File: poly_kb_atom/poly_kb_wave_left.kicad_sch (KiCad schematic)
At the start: 49 parts, among them U1 Pico, U2 TD6811, U3 MT9700

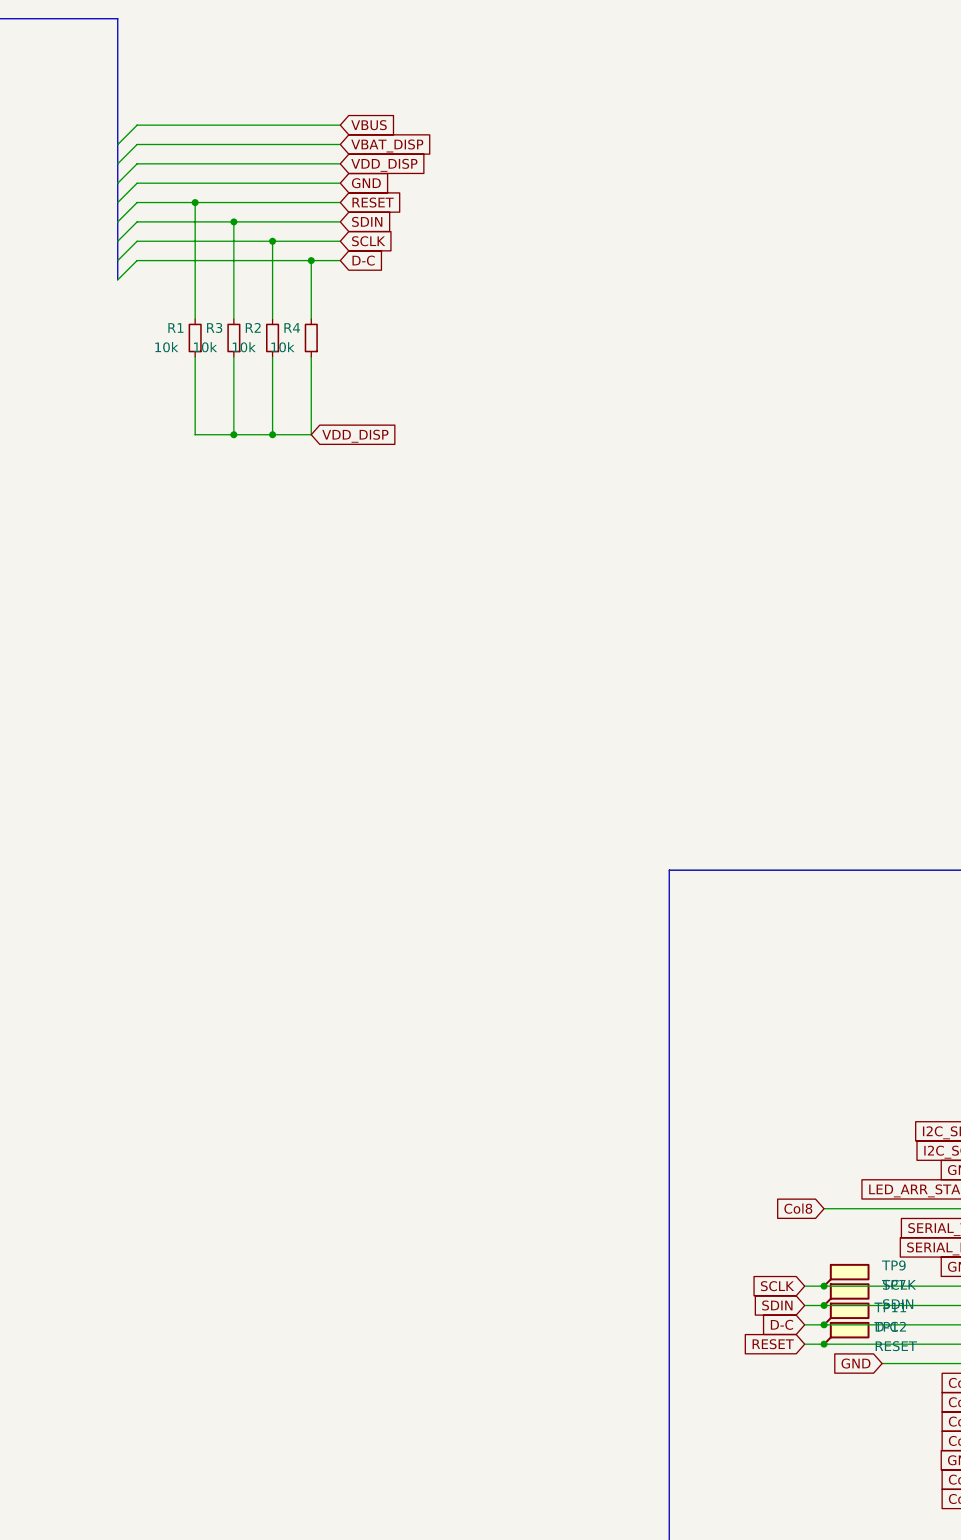
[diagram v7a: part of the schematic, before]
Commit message: Optional termination resistors
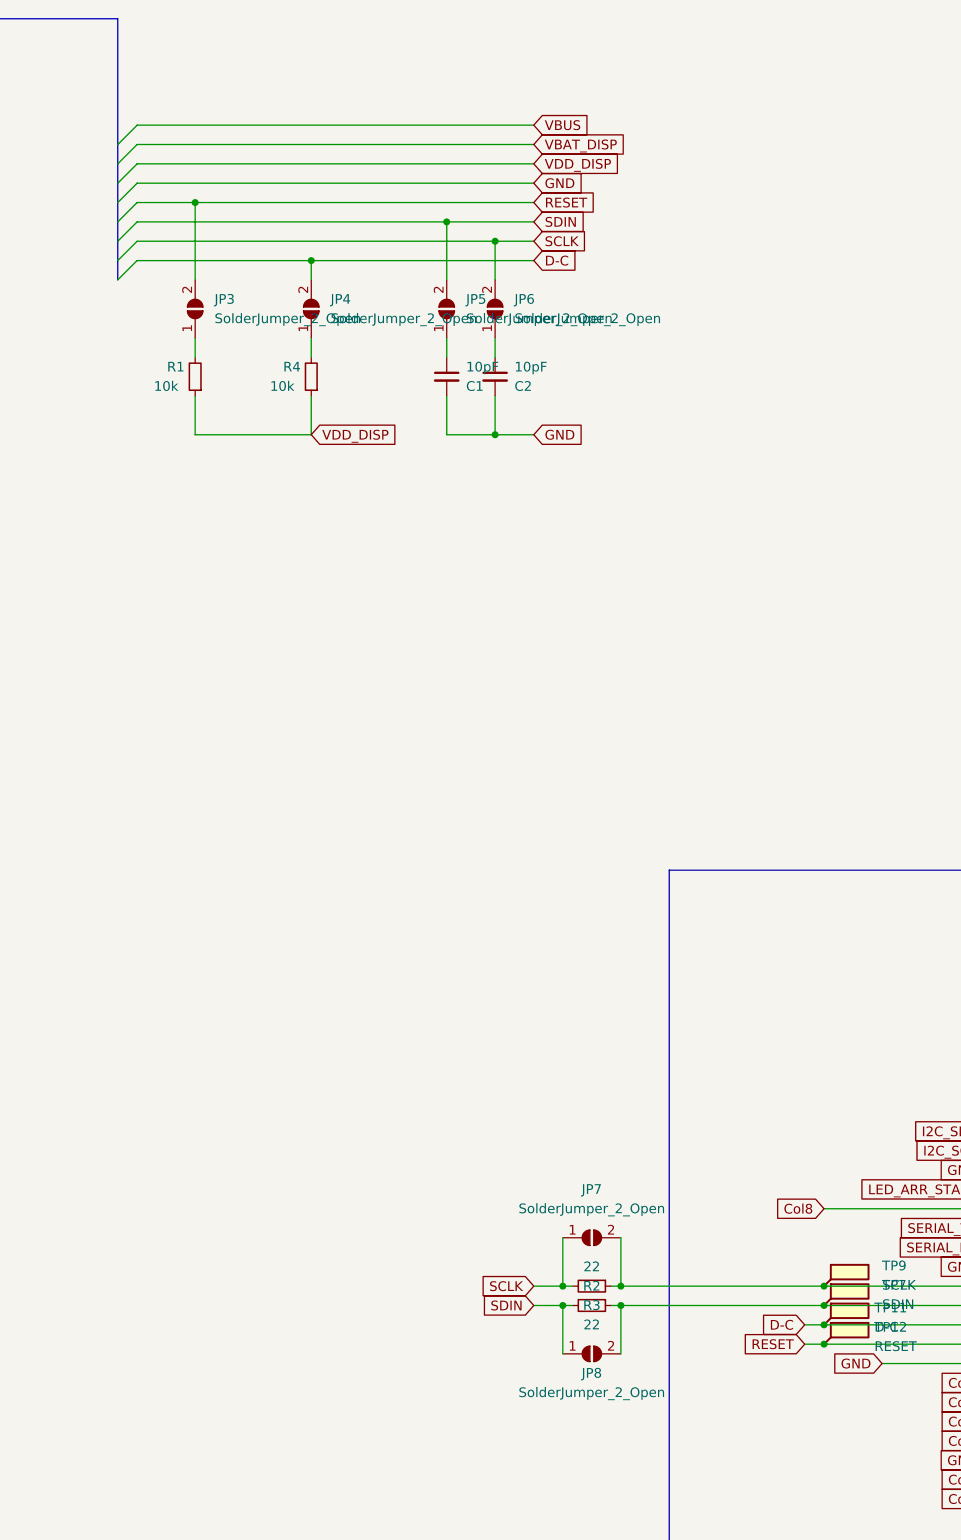
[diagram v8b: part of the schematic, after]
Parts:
- added C1, C2: 10pF, Capacitor_SMD:C_0603_1608Metric, symbol Device:C_Small
- added JP3, JP4, JP5, JP6, JP7, JP8: SolderJumper_2_Open, Jumper:SolderJumper-2_P1.3mm_Open_RoundedPad1.0x1.5mm, symbol Jumper:SolderJumper_2_Open
- R1, R4: LCSC C25804 -> C23162
- R2, R3: value 10k -> 22; LCSC C25804 -> C23345
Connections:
- net D-C: now also JP4.2 (B); no longer R4.2
- net GND: now also C1.2, C2.2
- net RESET: now also JP3.2 (B); no longer R1.2
- net SCLK: now also JP6.2 (B), JP7.1 (A); no longer TP9.1, U1.9 (GPIO6)
- net SDIN: now also JP5.2 (B), JP8.1 (A); no longer TP7.1, U1.10 (GPIO7)
- net VDD_DISP: no longer R2.1, R3.1
- new net: JP7.2 (B), R2.1, TP9.1, U1.9 (GPIO6)
- new net: JP4.1 (A), R4.2
- new net: C2.1, JP6.1 (A)
- new net: JP3.1 (A), R1.2
- new net: JP8.2 (B), R3.1, TP7.1, U1.10 (GPIO7)
- new net: C1.1, JP5.1 (A)
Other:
- moved on the sheet: R1, R4
